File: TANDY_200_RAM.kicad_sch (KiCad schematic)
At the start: 4 parts, among them J1 TANDY_26-3688, U1 62256_SOP28, U2 74LVC2G00

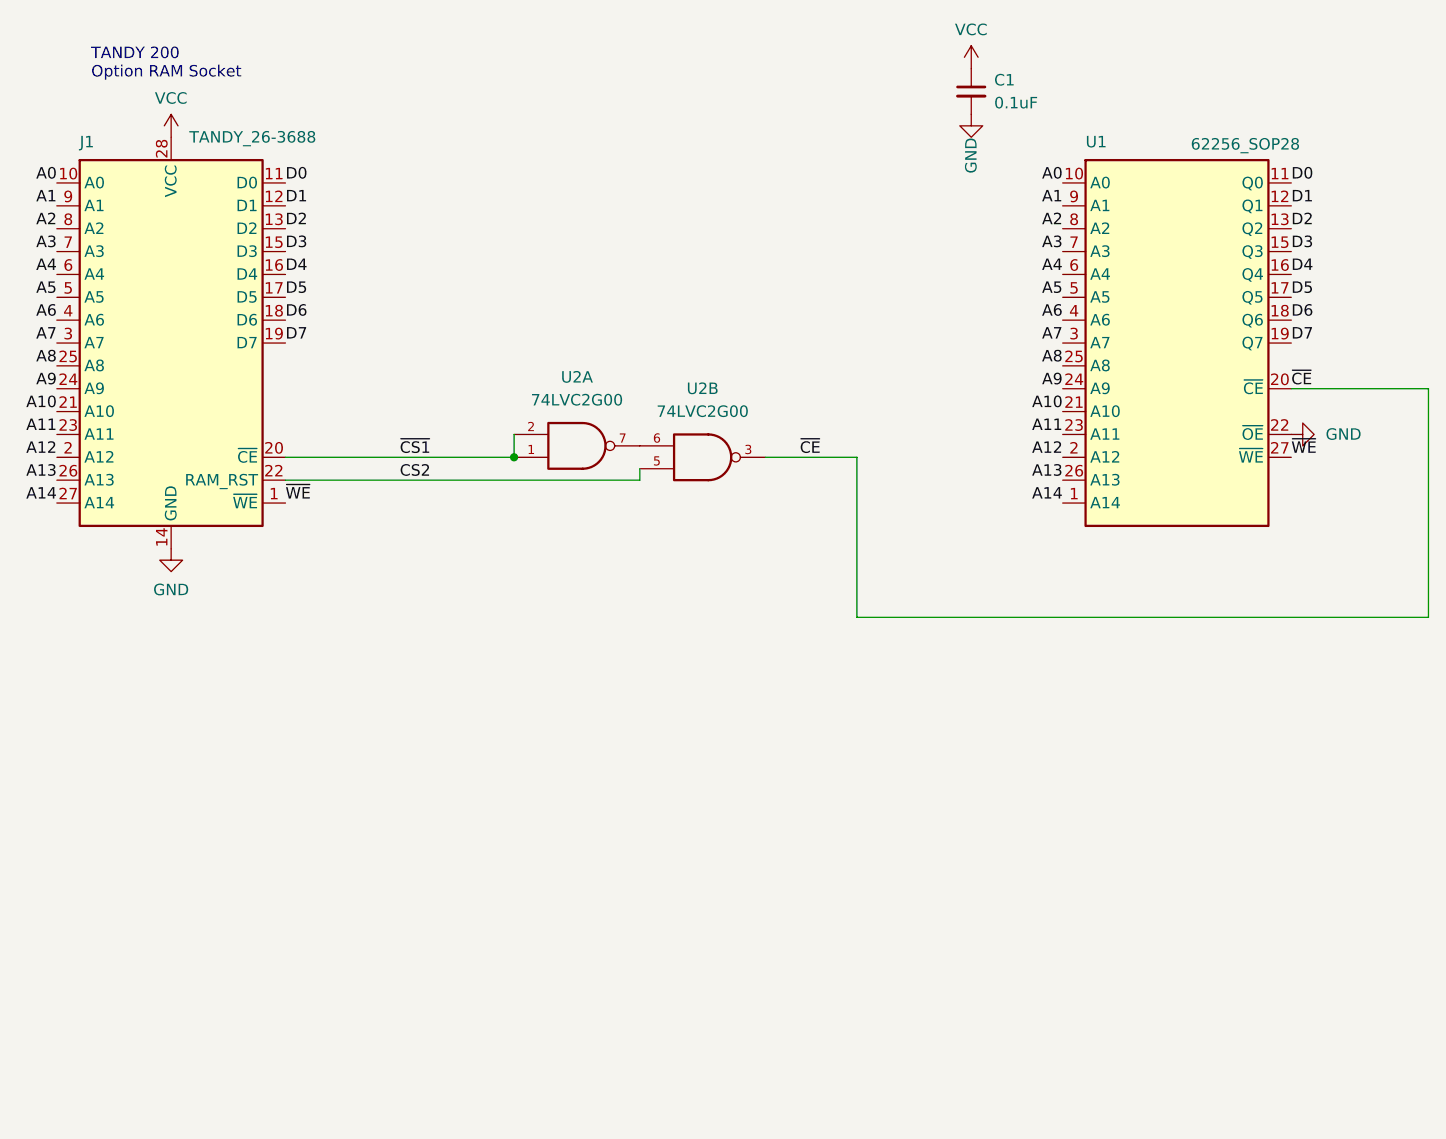
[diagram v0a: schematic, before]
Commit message: ground paths, footprints, sch symbols
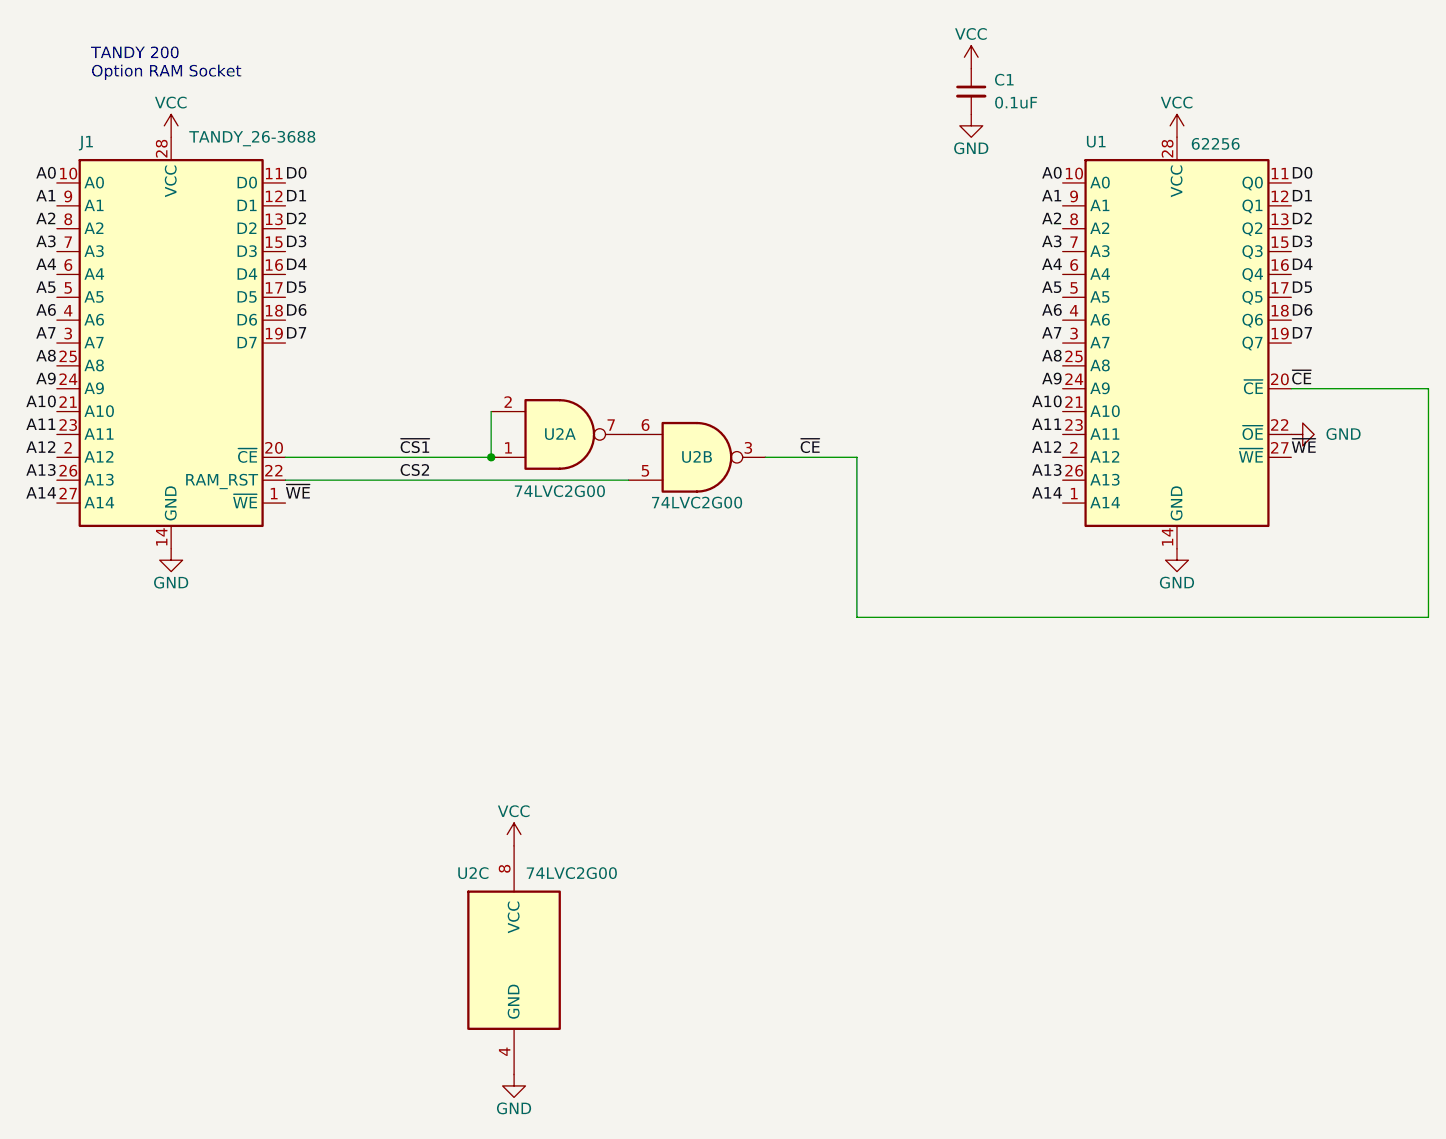
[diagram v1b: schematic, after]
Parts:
- added unit 3 of U2
- U1: value 62256_SOP28 -> 62256; symbol 000_LOCAL:62256_SOP28 -> 000_LOCAL:62256
- U2: footprint 000_LOCAL:SOT-505-2 -> 000_LOCAL:SSOP-8_2.95x2.8x0.65
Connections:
- net GND: now also U2.4 (GND); no longer U2.4 (GND), U2.4 (GND)
- net VCC: now also U2.8 (VCC); no longer U2.8 (VCC), U2.8 (VCC)

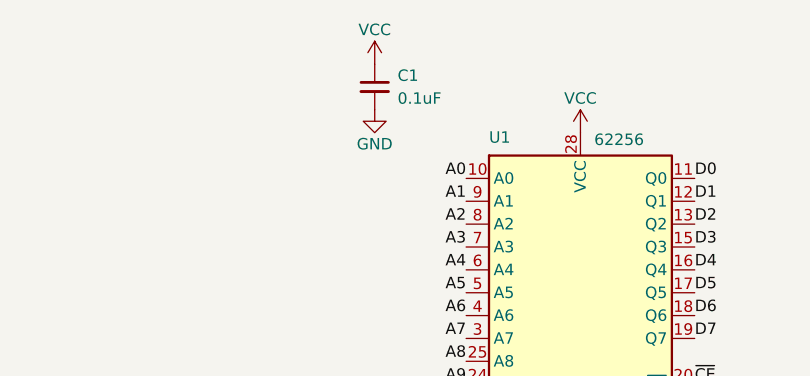
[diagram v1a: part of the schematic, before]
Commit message: 24k tsop layout and all board outlines expanded slightly
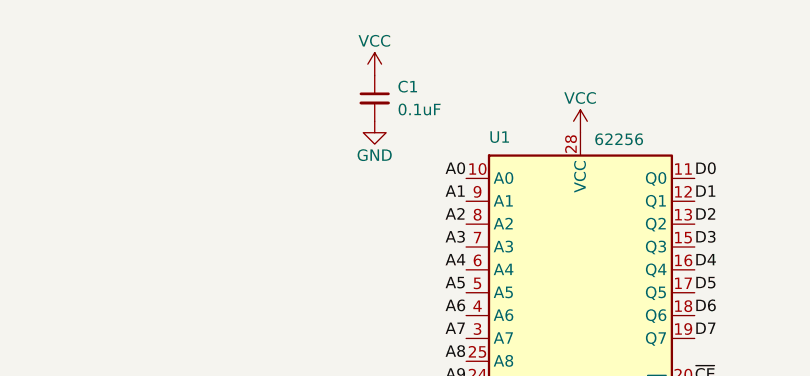
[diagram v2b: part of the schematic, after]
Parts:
- J1: footprint 000_LOCAL:KEL ICC05-028-360TP PCB -> 000_LOCAL:KEL ICC05-028-360TP
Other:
- moved on the sheet: C1
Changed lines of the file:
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@@
   (title_block
     (title "TANDY 200 RAM")
-    (date "2022-09-16")
-    (rev "001")
+    (date "2022-10-01")
+    (rev "002")
     (company "b.kenyon.w@gmail.com")
     (comment 1 "github.com/bkw777/TANDY_200_RAM")
@@
       (effects (font (size 1.27 1.27)) (justify left))
     )
-    (property "Footprint" "000_LOCAL:KEL ICC05-028-360TP PCB" (id 2) (at 76.2 99.06 0)
+    (property "Footprint" "000_LOCAL:KEL ICC05-028-360TP" (id 2) (at 76.2 99.06 0)
       (effects (font (size 1.27 1.27)) hide)
     )
@@
     (pin "1")
   )
-  (symbol (lib_id "power:VCC") (at 165.1 66.04 0) (unit 1)
-    (in_bom yes) (on_board yes)
-    (property "Reference" "#PWR0106" (id 0) (at 165.1 69.85 0)
-      (effects (font (size 1.27 1.27)) hide)
-    )
-    (property "Value" "VCC" (id 1) (at 165.1 62.23 0))
-    (property "Footprint" "" (id 2) (at 165.1 66.04 0)
-      (effects (font (size 1.27 1.27)) hide)
-    )
-    (property "Datasheet" "" (id 3) (at 165.1 66.04 0)
-      (effects (font (size 1.27 1.27)) hide)
-    )
-    (pin "1")
-  )
-  (symbol (lib_id "power:GND") (at 165.1 71.12 0) (unit 1)
-    (in_bom yes) (on_board yes)
-    (property "Reference" "#PWR0105" (id 0) (at 165.1 77.47 0)
-      (effects (font (size 1.27 1.27)) hide)
-    )
-    (property "Value" "GND" (id 1) (at 165.1 74.93 0))
-    (property "Footprint" "" (id 2) (at 165.1 71.12 0)
-      (effects (font (size 1.27 1.27)) hide)
-    )
-    (property "Datasheet" "" (id 3) (at 165.1 71.12 0)
-      (effects (font (size 1.27 1.27)) hide)
-    )
-    (pin "1")
-  )
-  (symbol (lib_id "000_LOCAL:C") (at 165.1 68.58 0) (unit 1)
+  (symbol (lib_id "power:VCC") (at 165.1 67.31 0) (unit 1)
+    (in_bom yes) (on_board yes)
+    (property "Reference" "#PWR0106" (id 0) (at 165.1 71.12 0)
+      (effects (font (size 1.27 1.27)) hide)
+    )
+    (property "Value" "VCC" (id 1) (at 165.1 63.5 0))
+    (property "Footprint" "" (id 2) (at 165.1 67.31 0)
+      (effects (font (size 1.27 1.27)) hide)
+    )
+    (property "Datasheet" "" (id 3) (at 165.1 67.31 0)
+      (effects (font (size 1.27 1.27)) hide)
+    )
+    (pin "1")
+  )
+  (symbol (lib_id "power:GND") (at 165.1 72.39 0) (unit 1)
+    (in_bom yes) (on_board yes)
+    (property "Reference" "#PWR0105" (id 0) (at 165.1 78.74 0)
+      (effects (font (size 1.27 1.27)) hide)
+    )
+    (property "Value" "GND" (id 1) (at 165.1 76.2 0))
+    (property "Footprint" "" (id 2) (at 165.1 72.39 0)
+      (effects (font (size 1.27 1.27)) hide)
+    )
+    (property "Datasheet" "" (id 3) (at 165.1 72.39 0)
+      (effects (font (size 1.27 1.27)) hide)
+    )
+    (pin "1")
+  )
+  (symbol (lib_id "000_LOCAL:C") (at 165.1 69.85 0) (unit 1)
     (in_bom yes) (on_board yes) (fields_autoplaced)
-    (property "Reference" "C1" (id 0) (at 167.64 67.3162 0)
+    (property "Reference" "C1" (id 0) (at 167.64 68.5862 0)
       (effects (font (size 1.27 1.27)) (justify left))
     )
-    (property "Value" "0.1uF" (id 1) (at 167.64 69.8562 0)
+    (property "Value" "0.1uF" (id 1) (at 167.64 71.1262 0)
       (effects (font (size 1.27 1.27)) (justify left))
     )
-    (property "Footprint" "000_LOCAL:C_0805" (id 2) (at 165.1 68.58 0)
-      (effects (font (size 1.27 1.27)) hide)
-    )
-    (property "Datasheet" "~" (id 3) (at 165.1 68.58 0)
+    (property "Footprint" "000_LOCAL:C_0805" (id 2) (at 165.1 69.85 0)
+      (effects (font (size 1.27 1.27)) hide)
+    )
+    (property "Datasheet" "~" (id 3) (at 165.1 69.85 0)
       (effects (font (size 1.27 1.27)) hide)
     )
@@
     )
     (path "/0ca43401-3dca-436a-b184-791083c316bb"
-      (reference "J1") (unit 1) (value "TANDY_26-3688") (footprint "000_LOCAL:KEL ICC05-028-360TP PCB")
+      (reference "J1") (unit 1) (value "TANDY_26-3688") (footprint "000_LOCAL:KEL ICC05-028-360TP")
     )
     (path "/c63808ae-1f01-41cd-bf76-9618093de932"
